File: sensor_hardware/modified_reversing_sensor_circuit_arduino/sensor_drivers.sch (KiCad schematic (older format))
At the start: 27 parts, among them Q1 S8050-J3Y, Q2 S8050-J3Y, Q3 S8050-J3Y, Q4 S8050-J3Y, T1 Transformer_1P_1S, T2 Transformer_1P_1S, T3 Transformer_1P_1S, T4 Transformer_1P_1S, U3 4052

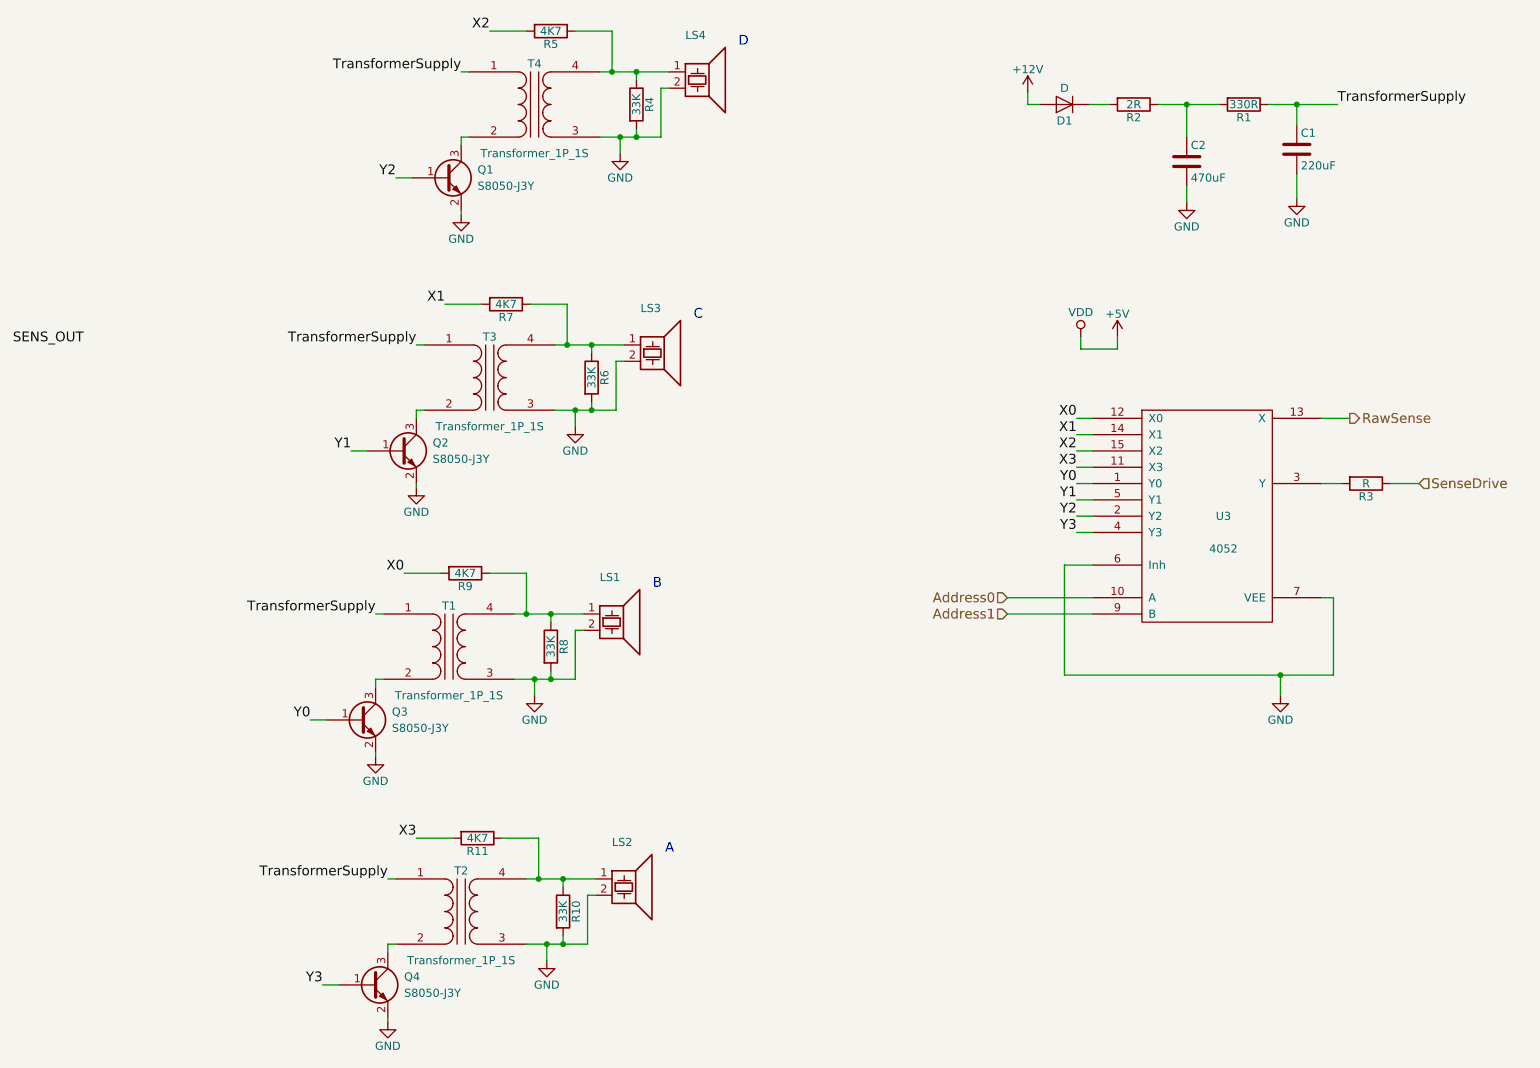
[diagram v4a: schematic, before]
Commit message: update readme and add wifi circuit details
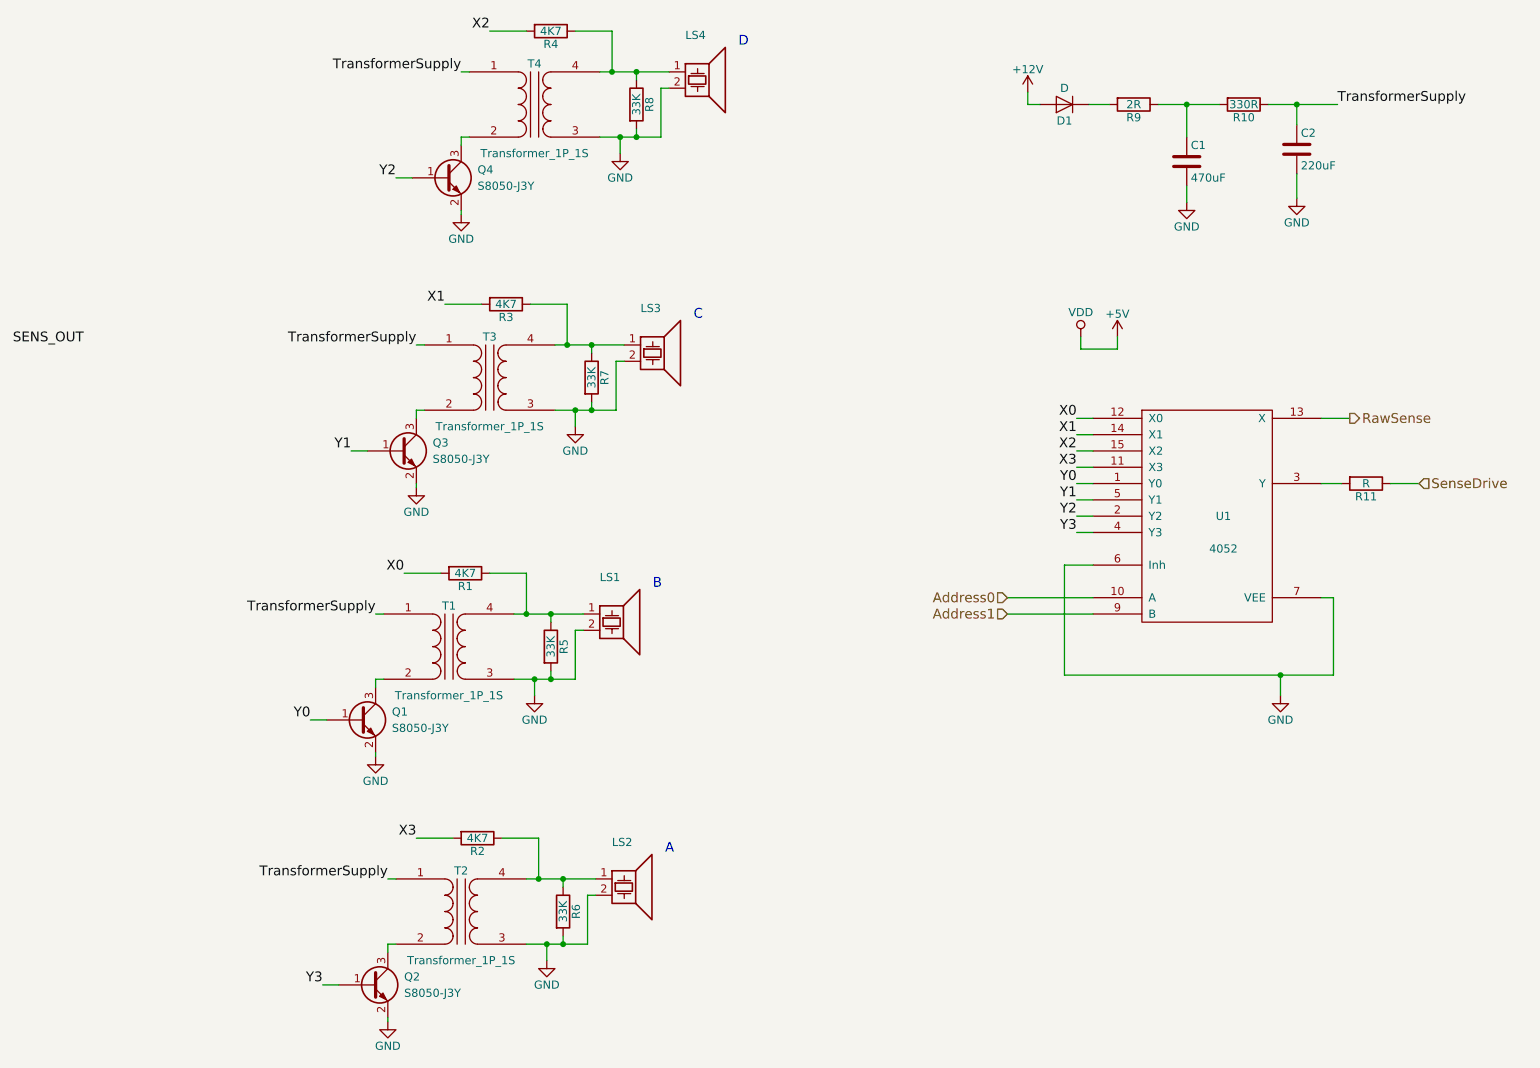
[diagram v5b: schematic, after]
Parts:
- renumbered C2 to C1, C1 to C2, Q3 to Q1, Q4 to Q2, Q2 to Q3, Q1 to Q4, R9 to R1, R1 to R10, R3 to R11, R11 to R2, R7 to R3, R5 to R4, R8 to R5, R10 to R6, R6 to R7, R4 to R8, R2 to R9, U3 to U1
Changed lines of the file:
@@
 LIBS:valves
 LIBS:atmega328p
+LIBS:esp-01
 LIBS:reversing_sensor_circuit-cache
 EELAYER 25 0
@@
 $Descr A4 11693 8268
 encoding utf-8
-Sheet 2 4
+Sheet 2 5
 Title ""
 Date ""
@@
 $EndDescr
 $Comp
-L R R1
+L R R10
 U 1 1 607248ED
 P 7575 1300
-F 0 "R1" V 7655 1300 50  0000 C CNN
+F 0 "R10" V 7655 1300 50  0000 C CNN
 F 1 "330R" V 7575 1300 50  0000 C CNN
 F 2 "" V 7505 1300 50  0001 C CNN
@@
 $EndComp
 $Comp
-L C C2
+L C C1
 U 1 1 607248F4
 P 7225 1650
-F 0 "C2" H 7250 1750 50  0000 L CNN
+F 0 "C1" H 7250 1750 50  0000 L CNN
 F 1 "470uF" H 7250 1550 50  0000 L CNN
 F 2 "" H 7263 1500 50  0001 C CNN
@@
 $EndComp
 $Comp
-L C C1
+L C C2
 U 1 1 607248FB
 P 7900 1575
-F 0 "C1" H 7925 1675 50  0000 L CNN
+F 0 "C2" H 7925 1675 50  0000 L CNN
 F 1 "220uF" H 7925 1475 50  0000 L CNN
 F 2 "" H 7938 1425 50  0001 C CNN
@@
 Connection ~ 3750 1500
 $Comp
-L R R4
+L R R8
 U 1 1 607251F5
 P 3850 1300
-F 0 "R4" V 3930 1300 50  0000 C CNN
+F 0 "R8" V 3930 1300 50  0000 C CNN
 F 1 "33K" V 3850 1300 50  0000 C CNN
 F 2 "" V 3780 1300 50  0001 C CNN
@@
 $EndComp
 $Comp
-L R R2
+L R R9
 U 1 1 60725829
 P 6900 1300
-F 0 "R2" V 6980 1300 50  0000 C CNN
+F 0 "R9" V 6980 1300 50  0000 C CNN
 F 1 "2R" V 6900 1300 50  0000 C CNN
 F 2 "" V 6830 1300 50  0001 C CNN
@@
 Connection ~ 3700 1100
 $Comp
-L R R5
+L R R4
 U 1 1 60728980
 P 3325 850
-F 0 "R5" V 3405 850 50  0000 C CNN
+F 0 "R4" V 3405 850 50  0000 C CNN
 F 1 "4K7" V 3325 850 50  0000 C CNN
 F 2 "" V 3255 850 50  0001 C CNN
@@
 	3175 850  2950 850
 $Comp
-L Q_NPN_BEC Q1
+L Q_NPN_BEC Q4
 U 1 1 60733E19
 P 2675 1750
-F 0 "Q1" H 2875 1800 50  0000 L CNN
+F 0 "Q4" H 2875 1800 50  0000 L CNN
 F 1 "S8050-J3Y" H 2875 1700 50  0000 L CNN
 F 2 "" H 2875 1850 50  0001 C CNN
@@
 Connection ~ 3475 3175
 $Comp
-L R R6
+L R R7
 U 1 1 6073CE8B
 P 3575 2975
-F 0 "R6" V 3655 2975 50  0000 C CNN
+F 0 "R7" V 3655 2975 50  0000 C CNN
 F 1 "33K" V 3575 2975 50  0000 C CNN
 F 2 "" V 3505 2975 50  0001 C CNN
@@
 Connection ~ 3425 2775
 $Comp
-L R R7
+L R R3
 U 1 1 6073CEA4
 P 3050 2525
-F 0 "R7" V 3130 2525 50  0000 C CNN
+F 0 "R3" V 3130 2525 50  0000 C CNN
 F 1 "4K7" V 3050 2525 50  0000 C CNN
 F 2 "" V 2980 2525 50  0001 C CNN
@@
 	2900 2525 2675 2525
 $Comp
-L Q_NPN_BEC Q2
+L Q_NPN_BEC Q3
 U 1 1 6073CEAC
 P 2400 3425
-F 0 "Q2" H 2600 3475 50  0000 L CNN
+F 0 "Q3" H 2600 3475 50  0000 L CNN
 F 1 "S8050-J3Y" H 2600 3375 50  0000 L CNN
 F 2 "" H 2600 3525 50  0001 C CNN
@@
 Connection ~ 3225 4825
 $Comp
-L R R8
+L R R5
 U 1 1 6073CFD3
 P 3325 4625
-F 0 "R8" V 3405 4625 50  0000 C CNN
+F 0 "R5" V 3405 4625 50  0000 C CNN
 F 1 "33K" V 3325 4625 50  0000 C CNN
 F 2 "" V 3255 4625 50  0001 C CNN
@@
 Connection ~ 3175 4425
 $Comp
-L R R9
+L R R1
 U 1 1 6073CFEC
 P 2800 4175
-F 0 "R9" V 2880 4175 50  0000 C CNN
+F 0 "R1" V 2880 4175 50  0000 C CNN
 F 1 "4K7" V 2800 4175 50  0000 C CNN
 F 2 "" V 2730 4175 50  0001 C CNN
@@
 	2650 4175 2425 4175
 $Comp
-L Q_NPN_BEC Q3
+L Q_NPN_BEC Q1
 U 1 1 6073CFF4
 P 2150 5075
-F 0 "Q3" H 2350 5125 50  0000 L CNN
+F 0 "Q1" H 2350 5125 50  0000 L CNN
 F 1 "S8050-J3Y" H 2350 5025 50  0000 L CNN
 F 2 "" H 2350 5175 50  0001 C CNN
@@
 Connection ~ 3300 6450
 $Comp
-L R R10
+L R R6
 U 1 1 6073D135
 P 3400 6250
-F 0 "R10" V 3480 6250 50  0000 C CNN
+F 0 "R6" V 3480 6250 50  0000 C CNN
 F 1 "33K" V 3400 6250 50  0000 C CNN
 F 2 "" V 3330 6250 50  0001 C CNN
@@
 Connection ~ 3250 6050
 $Comp
-L R R11
+L R R2
 U 1 1 6073D14E
 P 2875 5800
-F 0 "R11" V 2955 5800 50  0000 C CNN
+F 0 "R2" V 2955 5800 50  0000 C CNN
 F 1 "4K7" V 2875 5800 50  0000 C CNN
 F 2 "" V 2805 5800 50  0001 C CNN
@@
 	2725 5800 2500 5800
 $Comp
-L Q_NPN_BEC Q4
+L Q_NPN_BEC Q2
 U 1 1 6073D156
 P 2225 6700
-F 0 "Q4" H 2425 6750 50  0000 L CNN
+F 0 "Q2" H 2425 6750 50  0000 L CNN
 F 1 "S8050-J3Y" H 2425 6650 50  0000 L CNN
 F 2 "" H 2425 6800 50  0001 C CNN
@@
 	2325 6925 2325 6900
 $Comp
-L 4052 U3
+L 4052 U1
 U 1 1 6073F95B
 P 7350 3825
-F 0 "U3" H 7450 3825 50  0000 C CNN
+F 0 "U1" H 7450 3825 50  0000 C CNN
 F 1 "4052" H 7450 3625 50  0000 C CNN
 F 2 "" H 7350 3825 60  0001 C CNN
@@
 	8050 4325 8125 4325
 Wire Wire Line
-	8125 4800 8125 4325
-Wire Wire Line
-	6475 4800 8125 4800
+	8125 4325 8125 4800
+Wire Wire Line
+	8125 4800 6475 4800
 Wire Wire Line
 	7800 4800 7800 4925
@@
 $EndComp
 $Comp
-L R R3
+L R R11
 U 1 1 61413331
 P 8325 3625
-F 0 "R3" V 8405 3625 50  0000 C CNN
+F 0 "R11" V 8405 3625 50  0000 C CNN
 F 1 "R" V 8325 3625 50  0000 C CNN
 F 2 "" V 8255 3625 50  0001 C CNN
